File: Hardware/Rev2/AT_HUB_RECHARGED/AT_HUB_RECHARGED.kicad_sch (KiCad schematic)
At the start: 32 parts, among them J1 ESP Current SNS, SW1 SW_Push, SW10 SW_Push, SW2 SW_Push, SW3 SW_Push, SW4 SW_Push, SW5 SW_Push, SW6 SW_Push, SW7 SW_Push, SW8 SW_Push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

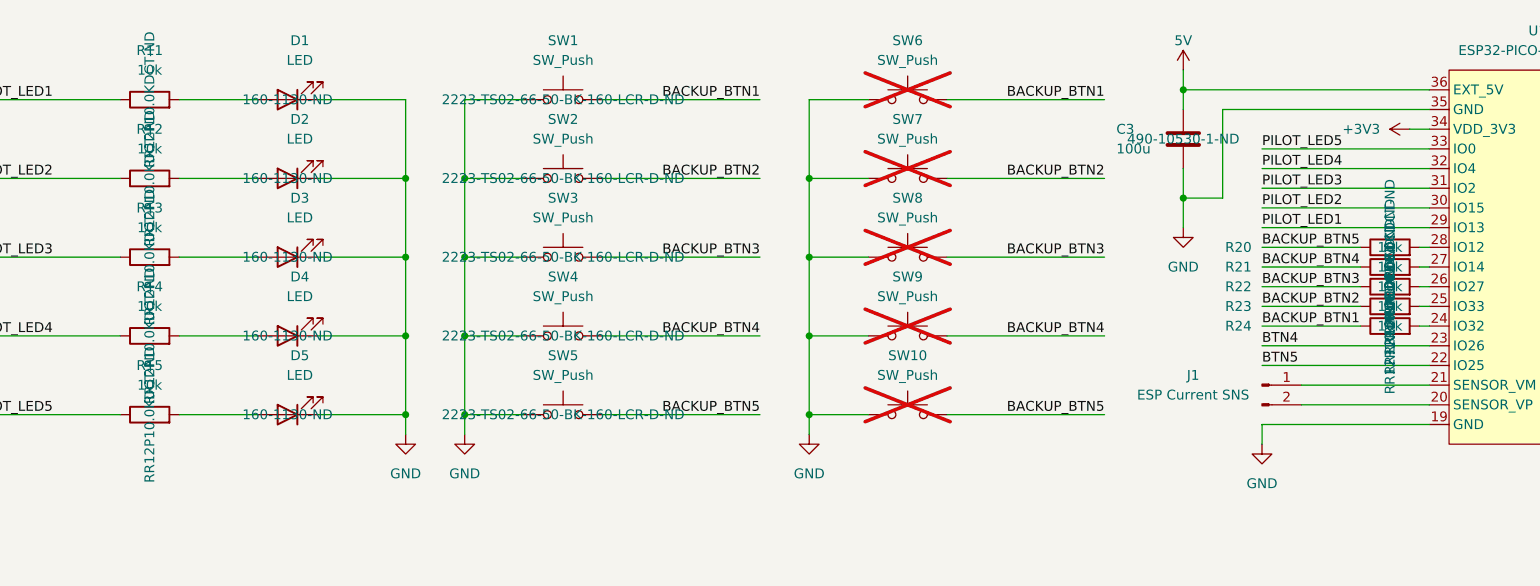
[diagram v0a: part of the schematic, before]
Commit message: Added new protections and load sharing for lipo, also changed inductor to be autoplaced
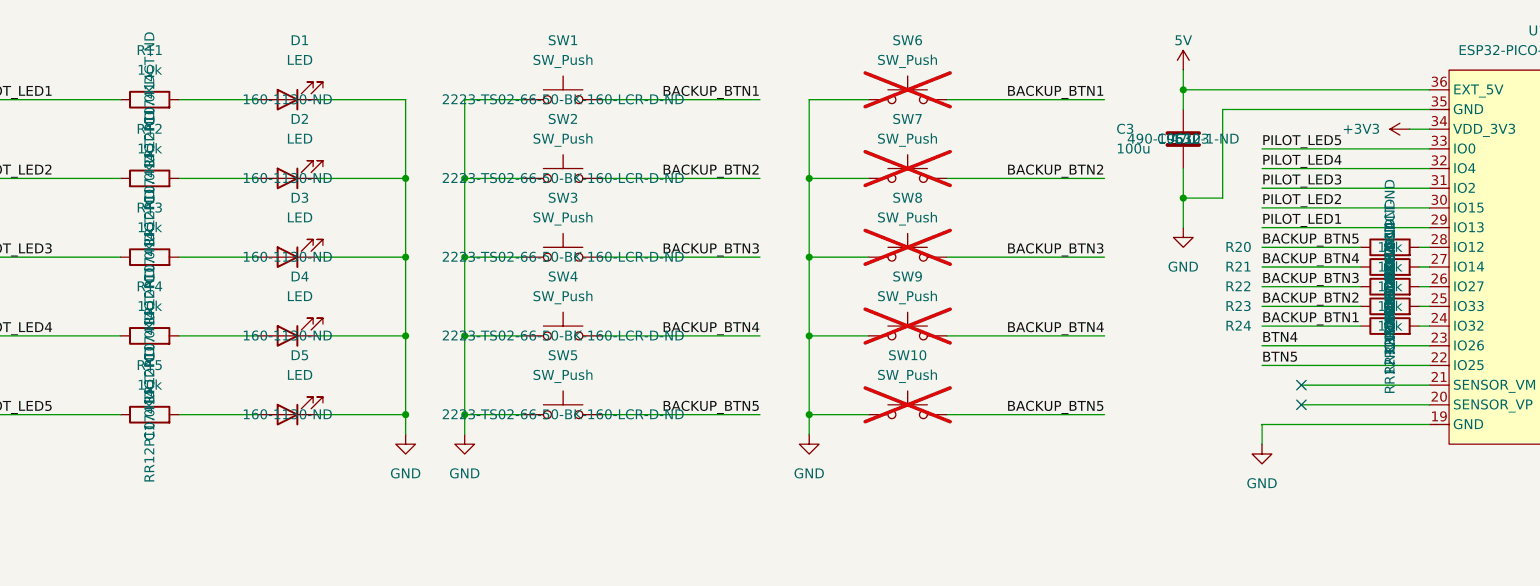
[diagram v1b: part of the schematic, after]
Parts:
- removed J1: ESP Current SNS, Connector_PinHeader_2.54mm:PinHeader_1x02_P2.54mm_Vertical, symbol Connector:Conn_01x02_Pin
- C3: footprint Capacitor_SMD:C_1210_3225Metric -> Capacitor_SMD:C_1206_3216Metric; Adjusted Value for stock (none) -> 47u; LCSC (none) -> C96123
- R11, R12, R13, R14, R15, R20, R21, R22, R23, R24: LCSC (none) -> C17414
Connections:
- no-connect marks 5 -> 7

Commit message: Done the design will verify
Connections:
- net BTN5: now also U1.15 (IO37); no longer U1.22 (IO25)
- net RELAY2: now also U1.22 (IO25); no longer U1.15 (IO37)
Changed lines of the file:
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@@
 	)
 	(label "BTN5"
-		(at 191.77 69.85 0)
+		(at 255.27 41.91 180)
 		(effects
 			(font
 				(size 1.27 1.27)
 			)
-			(justify left bottom)
+			(justify right bottom)
 		)
 	)
@@
 	)
 	(label "RELAY2"
-		(at 255.27 41.91 180)
+		(at 191.77 69.85 0)
 		(effects
 			(font
 				(size 1.27 1.27)
 			)
-			(justify right bottom)
+			(justify left bottom)
 		)
 	)
